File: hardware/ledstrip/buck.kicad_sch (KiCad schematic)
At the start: 5 parts, among them U3 TPS62162DSG

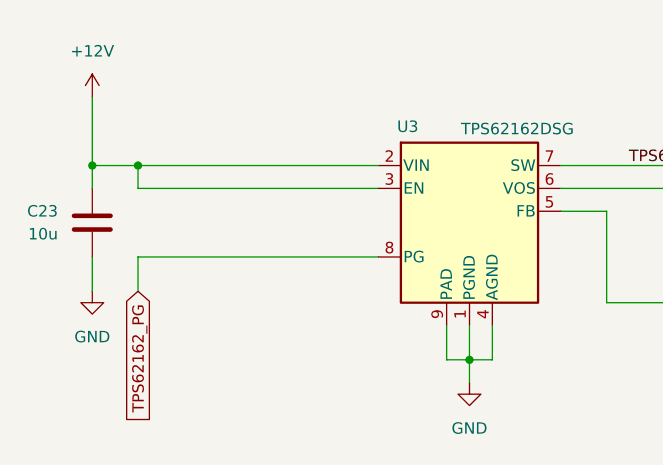
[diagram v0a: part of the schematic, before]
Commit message: Add a lot of TestPoints
Move P-FET at the edge of board.
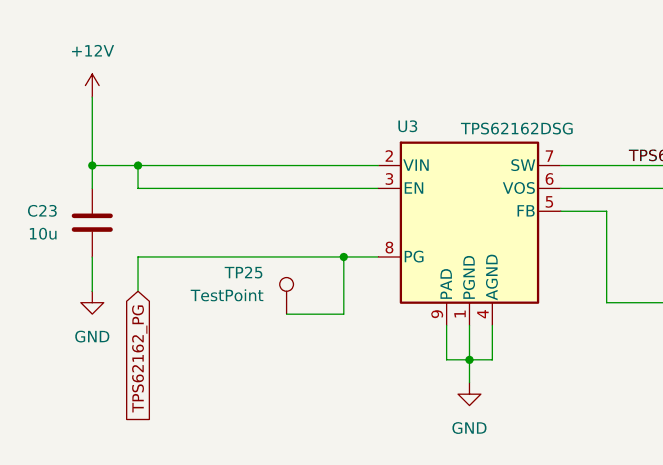
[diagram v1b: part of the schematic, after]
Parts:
- added TP25: TestPoint, TestPoint:TestPoint_Pad_1.0x1.0mm, symbol Connector:TestPoint
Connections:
- net TPS62162_PG: now also TP25.1
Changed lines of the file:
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@@
 		(color 0 0 0 0)
 	)
+	(junction
+		(at 118.11 88.9)
+		(diameter 0)
+		(color 0 0 0 0)
+	)
 	(wire
 		(pts
@@
 	(wire
 		(pts
+			(xy 118.11 88.9) (xy 121.92 88.9)
+		)
+		(stroke
+			(width 0)
+			(type default)
+		)
+	)
+	(wire
+		(pts
 			(xy 134.62 100.33) (xy 132.08 100.33)
 		)
@@
 	(wire
 		(pts
-			(xy 95.25 88.9) (xy 121.92 88.9)
+			(xy 95.25 88.9) (xy 118.11 88.9)
 		)
 		(stroke
@@
 	(wire
 		(pts
+			(xy 118.11 95.25) (xy 118.11 88.9)
+		)
+		(stroke
+			(width 0)
+			(type default)
+		)
+	)
+	(wire
+		(pts
 			(xy 186.69 93.98) (xy 186.69 100.33)
 		)
@@
 		(pts
 			(xy 95.25 81.28) (xy 121.92 81.28)
+		)
+		(stroke
+			(width 0)
+			(type default)
+		)
+	)
+	(wire
+		(pts
+			(xy 111.76 95.25) (xy 118.11 95.25)
 		)
 		(stroke
@@
 					(unit 1)
 				)
+			)
+		)
+	)
+	(symbol
+		(lib_id "Connector:TestPoint")
+		(at 111.76 95.25 0)
+		(mirror y)
+		(unit 1)
+		(exclude_from_sim no)
+		(in_bom yes)
+		(on_board yes)
+		(dnp no)
+		(property "Reference" "TP25"
+			(at 109.22 90.6779 0)
+			(effects
+				(font
+					(size 1.27 1.27)
+				)
+				(justify left)
+			)
+		)
+		(property "Value" "TestPoint"
+			(at 109.22 93.2179 0)
+			(effects
+				(font
+					(size 1.27 1.27)
+				)
+				(justify left)
+			)
+		)
+		(property "Footprint" "TestPoint:TestPoint_Pad_1.0x1.0mm"
+			(at 106.68 95.25 0)
+			(effects
+				(font
+					(size 1.27 1.27)
+				)
+				(hide yes)
+			)
+		)
+		(property "Datasheet" "~"
+			(at 106.68 95.25 0)
+			(effects
+				(font
+					(size 1.27 1.27)
+				)
+				(hide yes)
+			)
+		)
+		(property "Description" "test point"
+			(at 111.76 95.25 0)
+			(effects
+				(font
+					(size 1.27 1.27)
+				)
+				(hide yes)
+			)
+		)
+		(pin "1"
+		)
+		(instances
+			(project "ledstrip"
+				(path "/dcb997ee-94c4-4df2-ba22-0e091735ddd7/bd9eeed2-8672-4045-93ab-4cabbdf274b0"
+					(reference "TP25")
+					(unit 1)
+				)

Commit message: Fix a wrong capa and add MPN and stuff to STUSB4500
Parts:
- C24: footprint Capacitor_SMD:C_0805_2012Metric -> Capacitor_SMD:C_0603_1608Metric; MPN CL21A106KAYNNN -> CL10Z226MS96PNC
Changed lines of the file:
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@@
 			)
 		)
-		(property "Footprint" "Capacitor_SMD:C_0805_2012Metric"
+		(property "Footprint" "Capacitor_SMD:C_0603_1608Metric"
 			(at 185.7248 88.9 0)
 			(effects
@@
 			)
 		)
-		(property "MPN" "CL21A106KAYNNN"
+		(property "MPN" "CL10Z226MS96PNC"
 			(at 186.69 85.09 0)
 			(effects

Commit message: Improve BOM: exclude uneeded parts, add some columns.
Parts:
- TP25: now left out of the parts list
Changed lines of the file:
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@@
+			)
+		)
+		(property "Disributor Link 1" ""
+			(at 186.69 85.09 0)
+			(effects
+				(font
+					(size 1.27 1.27)
+				)
+				(hide yes)
+			)
+		)
+		(property "Ditributor Link 1" ""
+			(at 186.69 85.09 0)
+			(effects
+				(font
+					(size 1.27 1.27)
+				)
+				(hide yes)
+			)
+		)
+		(property "Manufacturer Part Number" ""
+			(at 186.69 85.09 0)
+			(effects
+				(font
+					(size 1.27 1.27)
+				)
+				(hide yes)
 			)
 		)
@@
 			)
 		)
+		(property "Disributor Link 1" ""
+			(at 90.17 85.09 0)
+			(effects
+				(font
+					(size 1.27 1.27)
+				)
+				(hide yes)
+			)
+		)
+		(property "Ditributor Link 1" ""
+			(at 90.17 85.09 0)
+			(effects
+				(font
+					(size 1.27 1.27)
+				)
+				(hide yes)
+			)
+		)
+		(property "Manufacturer Part Number" ""
+			(at 90.17 85.09 0)
+			(effects
+				(font
+					(size 1.27 1.27)
+				)
+				(hide yes)
+			)
+		)
 		(pin "1"
 		)
@@
 		)
 		(property "MPN" "TPS62162DSGT"
+			(at 132.08 86.36 0)
+			(effects
+				(font
+					(size 1.27 1.27)
+				)
+				(hide yes)
+			)
+		)
+		(property "Disributor Link 1" ""
+			(at 132.08 86.36 0)
+			(effects
+				(font
+					(size 1.27 1.27)
+				)
+				(hide yes)
+			)
+		)
+		(property "Ditributor Link 1" ""
+			(at 132.08 86.36 0)
+			(effects
+				(font
+					(size 1.27 1.27)
+				)
+				(hide yes)
+			)
+		)
+		(property "Manufacturer Part Number" ""
 			(at 132.08 86.36 0)
 			(effects
@@
 			)
 		)
+		(property "Disributor Link 1" ""
+			(at 171.45 78.74 90)
+			(effects
+				(font
+					(size 1.27 1.27)
+				)
+				(hide yes)
+			)
+		)
+		(property "Ditributor Link 1" ""
+			(at 171.45 78.74 90)
+			(effects
+				(font
+					(size 1.27 1.27)
+				)
+				(hide yes)
+			)
+		)
+		(property "Manufacturer Part Number" ""
+			(at 171.45 78.74 90)
+			(effects
+				(font
+					(size 1.27 1.27)
+				)
+				(hide yes)
+			)
+		)
 		(pin "1"
 		)
@@
 		(unit 1)
 		(exclude_from_sim no)
-		(in_bom yes)
+		(in_bom no)
 		(on_board yes)
 		(dnp no)
@@
 		)
 		(property "Description" "test point"
+			(at 111.76 95.25 0)
+			(effects
+				(font
+					(size 1.27 1.27)
+				)
+				(hide yes)
+			)
+		)
+		(property "Disributor Link 1" ""
+			(at 111.76 95.25 0)
+			(effects
+				(font
+					(size 1.27 1.27)
+				)
+				(hide yes)
+			)
+		)
+		(property "Ditributor Link 1" ""
+			(at 111.76 95.25 0)
+			(effects
+				(font
+					(size 1.27 1.27)
+				)
+				(hide yes)
+			)
+		)
+		(property "Manufacturer Part Number" ""
 			(at 111.76 95.25 0)
 			(effects
@@
 			(at 180.34 71.12 0)
 			(effects
+				(font
+					(size 1.27 1.27)
+				)
+				(hide yes)
+			)
+		)
+		(property "Disributor Link 1" ""
+			(at 180.34 71.12 0)
+			(effects
+				(font
+					(size 1.27 1.27)
+				)
+				(hide yes)
+			)
+		)
+		(property "Ditributor Link 1" ""
+			(at 180.34 71.12 0)
+			(effects
+				(font
+					(size 1.27 1.27)
+				)
+				(hide yes)
+			)
+		)
+		(property "Manufacturer Part Number" ""
+			(at 180.34 71.12 0)
+			(effects
